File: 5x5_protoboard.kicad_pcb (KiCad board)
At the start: 2 copper layers, 50 x 50 mm, 95 parts, among them CON1 BARREL_JACK, CON2 USB-MINI-B, CON3 USB-MICRO, J1 PINS_3X1, J10 PINS_3X1, J11 PINS_3X1, J12 PINS_3X1, J13 PINS_3X1, J14 PINS_3X1, J15 PINS_3X1, J16 PINS_3X1, J17 PINS_3X1, J18 PINS_3X1, J19 PINS_3X1, J2 PINS_3X1, J20 PINS_3X1, J21 PINS_3X1, J22 PINS_3X1, J23 PINS_3X1, J24 PINS_3X1, J25 PINS_3X1, J26 PINS_3X1, J27 PINS_3X1, J28 PINS_3X1, J29 PINS_3X1, J3 PINS_3X1, J30 PINS_3X1, J31 PINS_3X1, J32 PINS_3X1, J33 PINS_3X1, J34 PINS_3X1, J35 PINS_3X1, J36 PINS_3X1, J37 PINS_3X1, J38 PINS_3X1, J39 PINS_3X1, J4 PINS_3X1, J40 PINS_3X1, J41 PINS_3X1, J42 PINS_3X1, J43 PINS_3X1, J44 PINS_3X1, J45 PINS_3X1, J46 PINS_3X1, J47 PINS_3X1, J48 PINS_3X1, J49 PINS_3X1, J5 PINS_3X1, J50 PINS_3X1, J51 PINS_3X1, J52 PINS_3X1, J53 PINS_3X1, J54 PINS_3X1, J55 PINS_3X1, J56 PINS_3X1, J57 PINS_3X1, J58 PINS_3X1, J59 PINS_3X1, J6 PINS_3X1, J60 PINS_3X1, J61 PINS_3X1, J62 PINS_3X1, J63 PINS_3X1, J64 PINS_3X1, J65 PINS_2X1, J7 PINS_3X1, J8 PINS_3X1, J9 PINS_3X1, P1 CONN_5, U1 7805

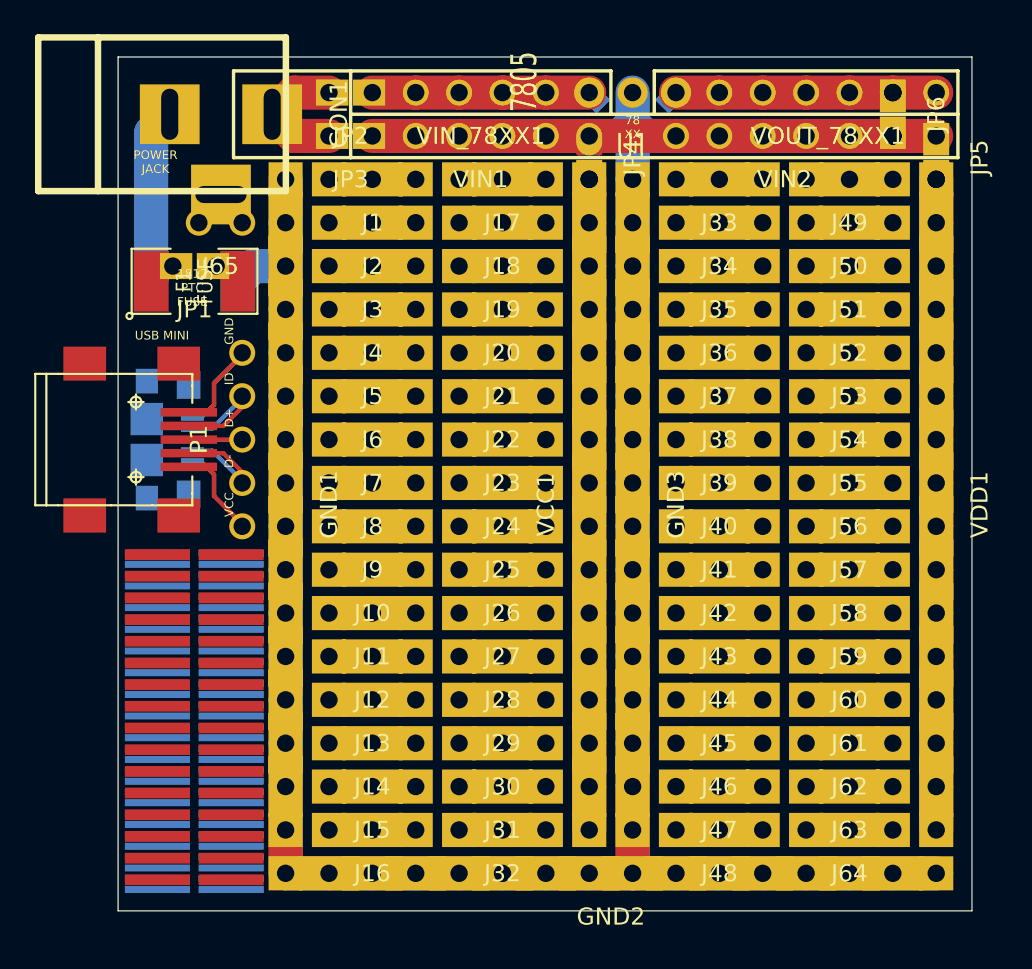
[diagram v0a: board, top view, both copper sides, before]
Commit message: changed interconnect to only have exposed copper on the bottom side, and shorted the jumper on the front side
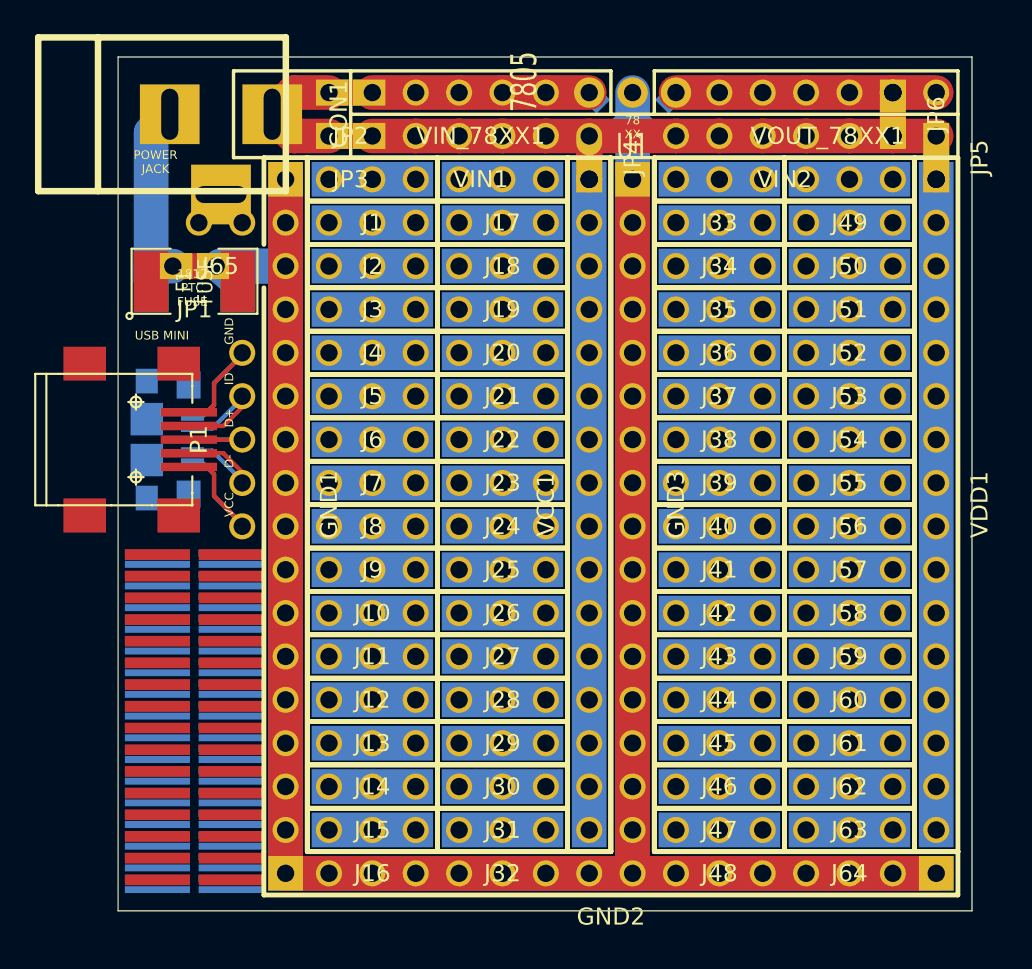
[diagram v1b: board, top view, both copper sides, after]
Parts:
- JP1, JP2, JP3, JP4, JP5, JP6: footprint PINS_RECT_2X1_SOLDER_JUMPER -> PINS_RECT_2X1_SOLDER_JUMPER_SHORTED_F
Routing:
- net N-0000083: track 137.8 -> 232.9 mm
- net N-0000041: track 38.1 -> 0.00 mm
- net N-0000040: track 38.1 -> 0.00 mm
- net N-0000054: track 10.2 -> 12.4 mm
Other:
- net class Power: trace_width 2 -> 2.032
